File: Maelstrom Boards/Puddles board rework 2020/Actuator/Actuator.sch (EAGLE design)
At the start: 75 parts, among them Q1 MOSFET-NCH-AO3404A, Q12 MOSFET-NCH-AO3404A, Q13 MOSFET-NCH-AO3404A, Q14 MOSFET-NCH-AO3404A, Q15 MOSFET-NCH-AO3404A, Q17 MOSFET-NCH-AO3404A, Q18 FDD4141TO252, Q2 MOSFET-NCH-AO3404A, Q3 MOSFET-NCH-AO3404A, Q4 MOSFET-NCH-AO3404A, Q5 MOSFET-NCH-AO3404A, Q6 FDD4141TO252, Y1 12MHz, Y3 32.768kHz

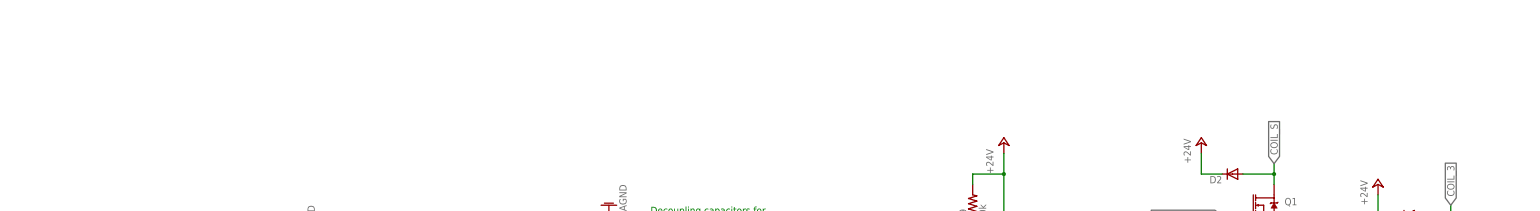
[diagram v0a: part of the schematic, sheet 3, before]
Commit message: Puddles board rework 2020: Battery Balancer and Actuator
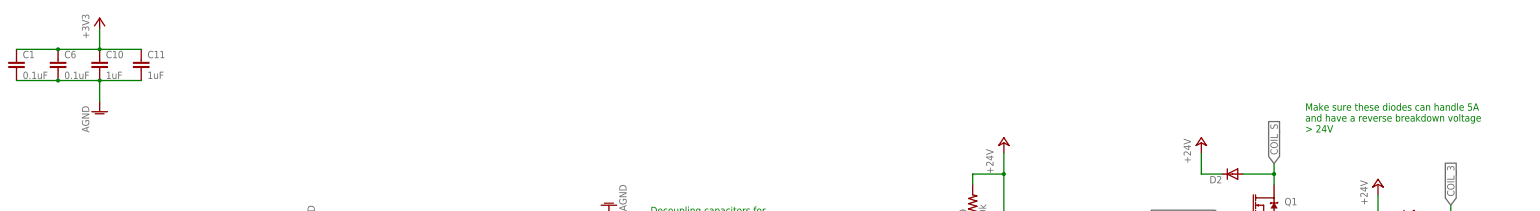
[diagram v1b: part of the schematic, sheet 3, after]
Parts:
- added C1, C6: 0.1uF, rcl:C-EUC0603
- added C10, C11: 1uF, rcl:C-EUC0603
- C5: device resistor:C-USC1206K -> rcl:C-EUC0603
- R10, R14, R17, R18, R19, R20, R22, R23, R24, R25, R26, R28: device resistor:R-US_R0805 -> rcl:R-US_R0603
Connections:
- net +12V: now also U$3.1+
- net +3V3: now also C1.1, C10.1, C11.1, C6.1
- net AGND: now also C1.2, C10.2, C11.2, C6.2, USB_ID/USB_DP/USB_DN.SHIELD
- net V+: no longer U$3.1+
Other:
- note added: "Make sure these diodes can handle 5A and have a reverse breakdown voltage > 24V"

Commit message: updates to puddles board rework actuator and BB.
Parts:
- removed C14: 1000 uF, rcl:CPOL-USE5-13
- removed CHARGING: (no value), led:LEDCHIPLED_0603
- removed R14: 100, rcl:R-US_R0603
- LIGHT1, LIGHT2, LIGHT3, LIGHT4, LIGHT5, LIGHT6, LIGHT7, LIGHT8: value (none) -> Red
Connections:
- removed net N$4: CHARGING.C, R14.2
- net +3V3: no longer CHARGING.A
- net AGND: no longer C14.-, R14.1
- net V+: no longer C14.+

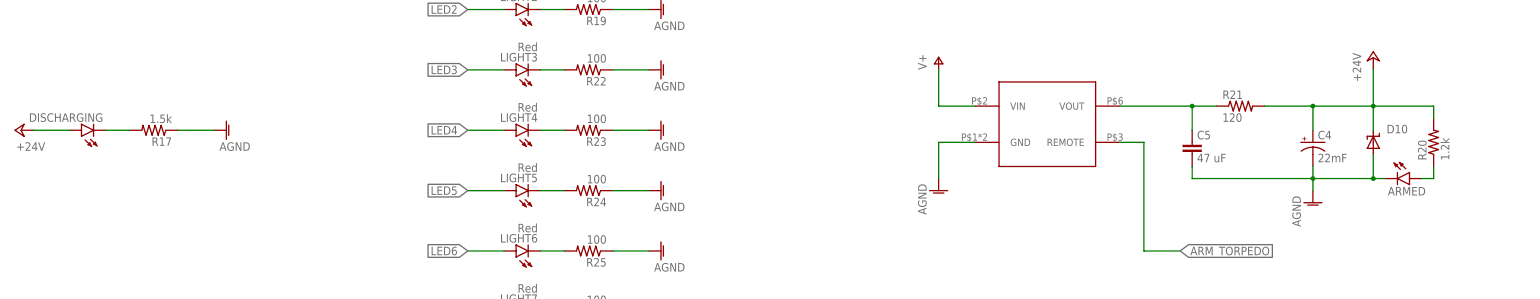
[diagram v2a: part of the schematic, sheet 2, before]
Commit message: updates to puddles acutator board. Resistor wattage concerns addressed
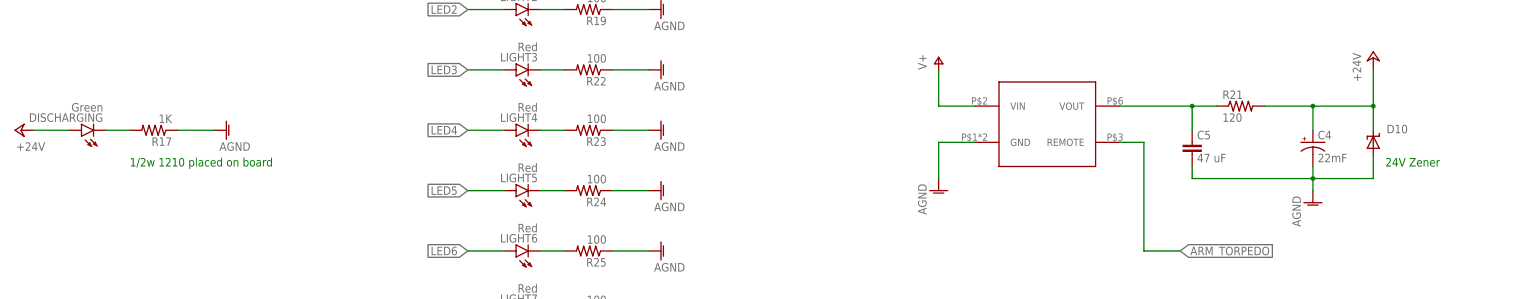
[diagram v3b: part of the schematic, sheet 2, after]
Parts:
- removed ARMED: (no value), led:LEDCHIPLED_0603
- removed R20: 1.2k, rcl:R-US_R0603
- DISCHARGING: value (none) -> Green
- R10: device rcl:R-US_R0603 -> rcl:R-US_R1210
- R17: value 1.5k -> 1K; device rcl:R-US_R0603 -> rcl:R-US_R1210
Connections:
- removed net N$10: ARMED.A, R20.1
- net +24V: no longer R20.2
- net AGND: no longer ARMED.C
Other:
- note added: "1/2w"
- note added: "1/2w 1210 placed on board"
- note added: "1210 placed on board"
- note added: "24V Zener"
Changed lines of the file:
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@@
 <part name="P+13" library="supply1" library_urn="urn:adsk.eagle:library:371" deviceset="V+" device=""/>
 <part name="BATTERY" library="led" library_urn="urn:adsk.eagle:library:259" deviceset="LED" device="CHIPLED_0603" package3d_urn="urn:adsk.eagle:package:15822/2"/>
-<part name="R10" library="rcl" library_urn="urn:adsk.eagle:library:334" deviceset="R-US_" device="R0603" package3d_urn="urn:adsk.eagle:package:23555/3" value="1.2k"/>
+<part name="R10" library="rcl" library_urn="urn:adsk.eagle:library:334" deviceset="R-US_" device="R1210" package3d_urn="urn:adsk.eagle:package:23554/2" value="1.2k"/>
 <part name="P+16" library="supply1" library_urn="urn:adsk.eagle:library:371" deviceset="+5V" device=""/>
 <part name="+3V6" library="supply1" library_urn="urn:adsk.eagle:library:371" deviceset="+3V3" device=""/>
@@
 <part name="P+8" library="supply1" library_urn="urn:adsk.eagle:library:371" deviceset="+24V" device=""/>
 <part name="U$6" library="converter" deviceset="TMR6-2415" device=""/>
-<part name="ARMED" library="led" library_urn="urn:adsk.eagle:library:259" deviceset="LED" device="CHIPLED_0603" package3d_urn="urn:adsk.eagle:package:15822/2"/>
-<part name="R20" library="rcl" library_urn="urn:adsk.eagle:library:334" deviceset="R-US_" device="R0603" package3d_urn="urn:adsk.eagle:package:23555/3" value="1.2k"/>
 <part name="R21" library="resistor" library_urn="urn:adsk.eagle:library:348" deviceset="R-US_" device="R6332W" package3d_urn="urn:adsk.eagle:package:26078/1" value="120"/>
 <part name="FRAME3" library="frames" library_urn="urn:adsk.eagle:library:229" deviceset="A3L-LOC" device="" value="a"/>
@@
 <part name="AGND4" library="supply1" library_urn="urn:adsk.eagle:library:371" deviceset="AGND" device=""/>
 <part name="+3V2" library="supply1" library_urn="urn:adsk.eagle:library:371" deviceset="+3V3" device=""/>
-<part name="DISCHARGING" library="led" library_urn="urn:adsk.eagle:library:259" deviceset="LED" device="CHIPLED_0603" package3d_urn="urn:adsk.eagle:package:15822/2"/>
+<part name="DISCHARGING" library="led" library_urn="urn:adsk.eagle:library:259" deviceset="LED" device="CHIPLED_0603" package3d_urn="urn:adsk.eagle:package:15822/2" value="Green"/>
 <part name="P+5" library="supply1" library_urn="urn:adsk.eagle:library:371" deviceset="+24V" device=""/>
-<part name="R17" library="rcl" library_urn="urn:adsk.eagle:library:334" deviceset="R-US_" device="R0603" package3d_urn="urn:adsk.eagle:package:23555/3" value="1.5k"/>
+<part name="R17" library="rcl" library_urn="urn:adsk.eagle:library:334" deviceset="R-US_" device="R1210" package3d_urn="urn:adsk.eagle:package:23554/2" value="1K"/>
 <part name="AGND16" library="supply1" library_urn="urn:adsk.eagle:library:371" deviceset="AGND" device=""/>
 <part name="AGND17" library="supply1" library_urn="urn:adsk.eagle:library:371" deviceset="AGND" device=""/>
@@
 Ohio State University</text>
 <text x="344.319859375" y="20.106640625" size="2.54" layer="94">Electrical Team</text>
+<text x="167.64" y="144.78" size="1.778" layer="91">1/2w</text>
+<text x="167.64" y="134.62" size="1.778" layer="91">1210 placed on board</text>
 </plain>
 <instances>
@@
 Ohio State University</text>
 <text x="344.319859375" y="20.106640625" size="2.54" layer="94">Electrical Team</text>
+<text x="320.04" y="185.42" size="1.778" layer="91">24V Zener</text>
+<text x="55.88" y="185.42" size="1.778" layer="91">1/2w 1210 placed on board</text>
 </plain>
 <instances>
@@
 </instance>
 <instance part="U$6" gate="G$1" x="238.76" y="185.42" smashed="yes"/>
-<instance part="ARMED" gate="G$1" x="325.12" y="182.88" smashed="yes" rot="R270">
-<attribute name="NAME" x="320.548" y="179.324" size="1.778" layer="95"/>
-<attribute name="VALUE" x="320.548" y="177.165" size="1.778" layer="96"/>
-</instance>
-<instance part="R20" gate="G$1" x="330.2" y="190.5" smashed="yes" rot="R90">
-<attribute name="NAME" x="328.7014" y="186.69" size="1.778" layer="95" rot="R90"/>
-<attribute name="VALUE" x="333.502" y="186.69" size="1.778" layer="96" rot="R90"/>
-</instance>
 <instance part="R21" gate="G$1" x="289.56" y="198.12" smashed="yes">
 <attribute name="NAME" x="285.75" y="199.6186" size="1.778" layer="95"/>
@@
 <wire x1="279.4" y1="185.42" x2="279.4" y2="182.88" width="0.1524" layer="91"/>
 <wire x1="279.4" y1="182.88" x2="304.8" y2="182.88" width="0.1524" layer="91"/>
-<pinref part="ARMED" gate="G$1" pin="C"/>
-<wire x1="320.04" y1="182.88" x2="317.5" y2="182.88" width="0.1524" layer="91"/>
-<junction x="317.5" y="182.88"/>
 </segment>
 <segment>
@@
 <wire x1="317.5" y1="198.12" x2="317.5" y2="205.74" width="0.1524" layer="91"/>
 <junction x="317.5" y="198.12"/>
-<wire x1="317.5" y1="198.12" x2="330.2" y2="198.12" width="0.1524" layer="91"/>
-<wire x1="330.2" y1="198.12" x2="330.2" y2="195.58" width="0.1524" layer="91"/>
-<pinref part="R20" gate="G$1" pin="2"/>
 <pinref part="R21" gate="G$1" pin="2"/>
 </segment>
@@
 </segment>
 </net>
-<net name="N$10" class="0">
-<segment>
-<wire x1="330.2" y1="185.42" x2="330.2" y2="182.88" width="0.1524" layer="91"/>
-<pinref part="ARMED" gate="G$1" pin="A"/>
-<wire x1="330.2" y1="182.88" x2="327.66" y2="182.88" width="0.1524" layer="91"/>
-<pinref part="R20" gate="G$1" pin="1"/>
-</segment>
-</net>

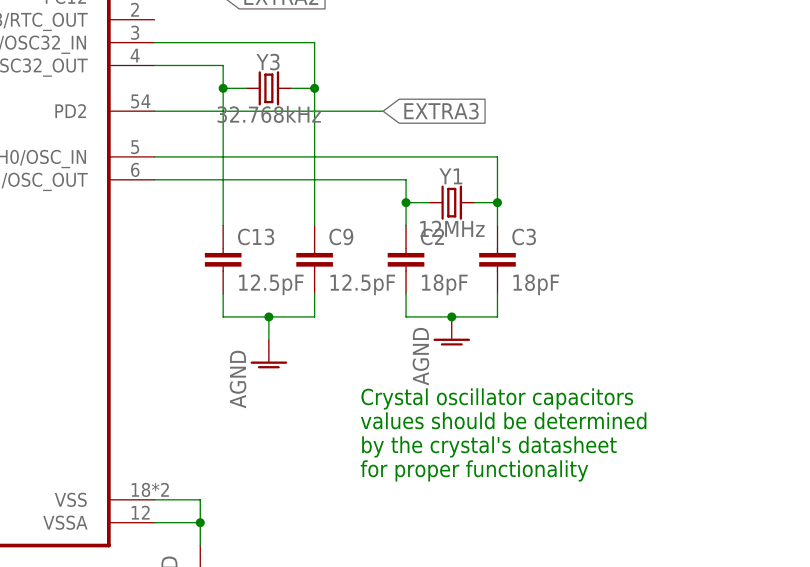
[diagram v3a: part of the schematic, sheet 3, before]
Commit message: Changing puddles actuator crystal caps
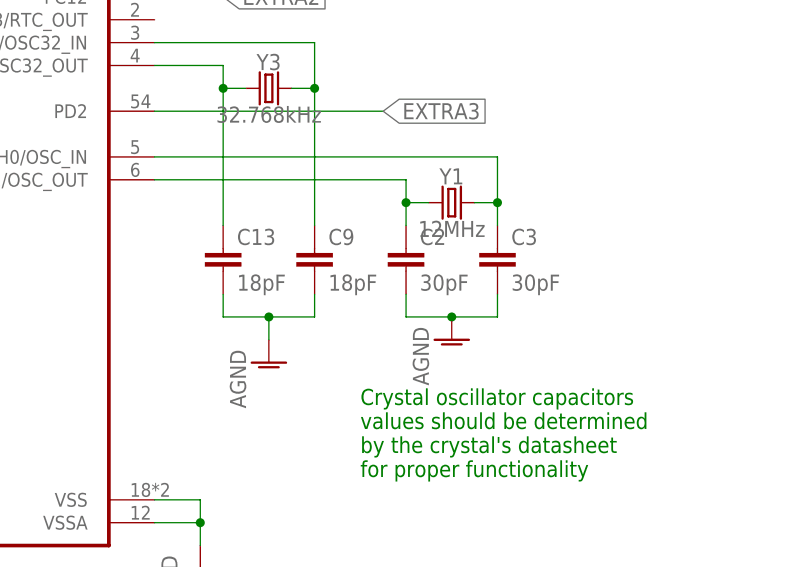
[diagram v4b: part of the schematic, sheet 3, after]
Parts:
- C13, C9: value 12.5pF -> 18pF
- C2, C3: value 18pF -> 30pF
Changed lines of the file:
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@@
 <?xml version="1.0" encoding="utf-8"?>
 <!DOCTYPE eagle SYSTEM "eagle.dtd">
-<eagle version="9.5.2">
+<eagle version="9.6.2">
 <drawing>
 <settings>
@@
 <part name="MC" library="STM32F405RGT6" deviceset="STM32F405RGT6" device=""/>
 <part name="Y1" library="SparkFun-Clocks" library_urn="urn:adsk.eagle:library:511" deviceset="CRYSTAL-16MHZ" device="PTH-HC49US" package3d_urn="urn:adsk.eagle:package:37515/1" value="12MHz"/>
-<part name="C2" library="rcl" library_urn="urn:adsk.eagle:library:334" deviceset="C-EU" device="C0603" package3d_urn="urn:adsk.eagle:package:23616/2" value="18pF"/>
-<part name="C3" library="rcl" library_urn="urn:adsk.eagle:library:334" deviceset="C-EU" device="C0603" package3d_urn="urn:adsk.eagle:package:23616/2" value="18pF"/>
+<part name="C2" library="rcl" library_urn="urn:adsk.eagle:library:334" deviceset="C-EU" device="C0603" package3d_urn="urn:adsk.eagle:package:23616/2" value="30pF"/>
+<part name="C3" library="rcl" library_urn="urn:adsk.eagle:library:334" deviceset="C-EU" device="C0603" package3d_urn="urn:adsk.eagle:package:23616/2" value="30pF"/>
 <part name="+3V15" library="supply1" library_urn="urn:adsk.eagle:library:371" deviceset="+3V3" device=""/>
 <part name="C7" library="rcl" library_urn="urn:adsk.eagle:library:334" deviceset="C-EU" device="C0603" package3d_urn="urn:adsk.eagle:package:23616/2" value="2.2uF"/>
@@
 <part name="RESET_SWITCH" library="SparkFun-Switches" library_urn="urn:adsk.eagle:library:535" deviceset="MOMENTARY-SWITCH-SPST" device="-PTH-6.0MM" package3d_urn="urn:adsk.eagle:package:40163/1"/>
 <part name="Y3" library="SparkFun-Clocks" library_urn="urn:adsk.eagle:library:511" deviceset="CRYSTAL-32.768KHZ" device="SMD-3.2X1.5" package3d_urn="urn:adsk.eagle:package:37548/1" value="32.768kHz"/>
-<part name="C13" library="rcl" library_urn="urn:adsk.eagle:library:334" deviceset="C-EU" device="C0603" package3d_urn="urn:adsk.eagle:package:23616/2" value="12.5pF"/>
-<part name="C9" library="rcl" library_urn="urn:adsk.eagle:library:334" deviceset="C-EU" device="C0603" package3d_urn="urn:adsk.eagle:package:23616/2" value="12.5pF"/>
+<part name="C13" library="rcl" library_urn="urn:adsk.eagle:library:334" deviceset="C-EU" device="C0603" package3d_urn="urn:adsk.eagle:package:23616/2" value="18pF"/>
+<part name="C9" library="rcl" library_urn="urn:adsk.eagle:library:334" deviceset="C-EU" device="C0603" package3d_urn="urn:adsk.eagle:package:23616/2" value="18pF"/>
 <part name="R27" library="rcl" library_urn="urn:adsk.eagle:library:334" deviceset="R-US_" device="R0603" package3d_urn="urn:adsk.eagle:package:23555/3" value="4.7k"/>
 <part name="+3V19" library="supply1" library_urn="urn:adsk.eagle:library:371" deviceset="+3V3" device=""/>
